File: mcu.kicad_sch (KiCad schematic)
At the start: 58 parts, among them P20 HEADER-2x11, P22 HEADER-2x13, P26 LPC_JTAG, P28 HEADER-2x11, SW1 SWITCH, SW2 SWITCH, U20 W25Q16, U23 LPC4330FET180, X2 MCU_XTAL, X3 RTC_XTAL

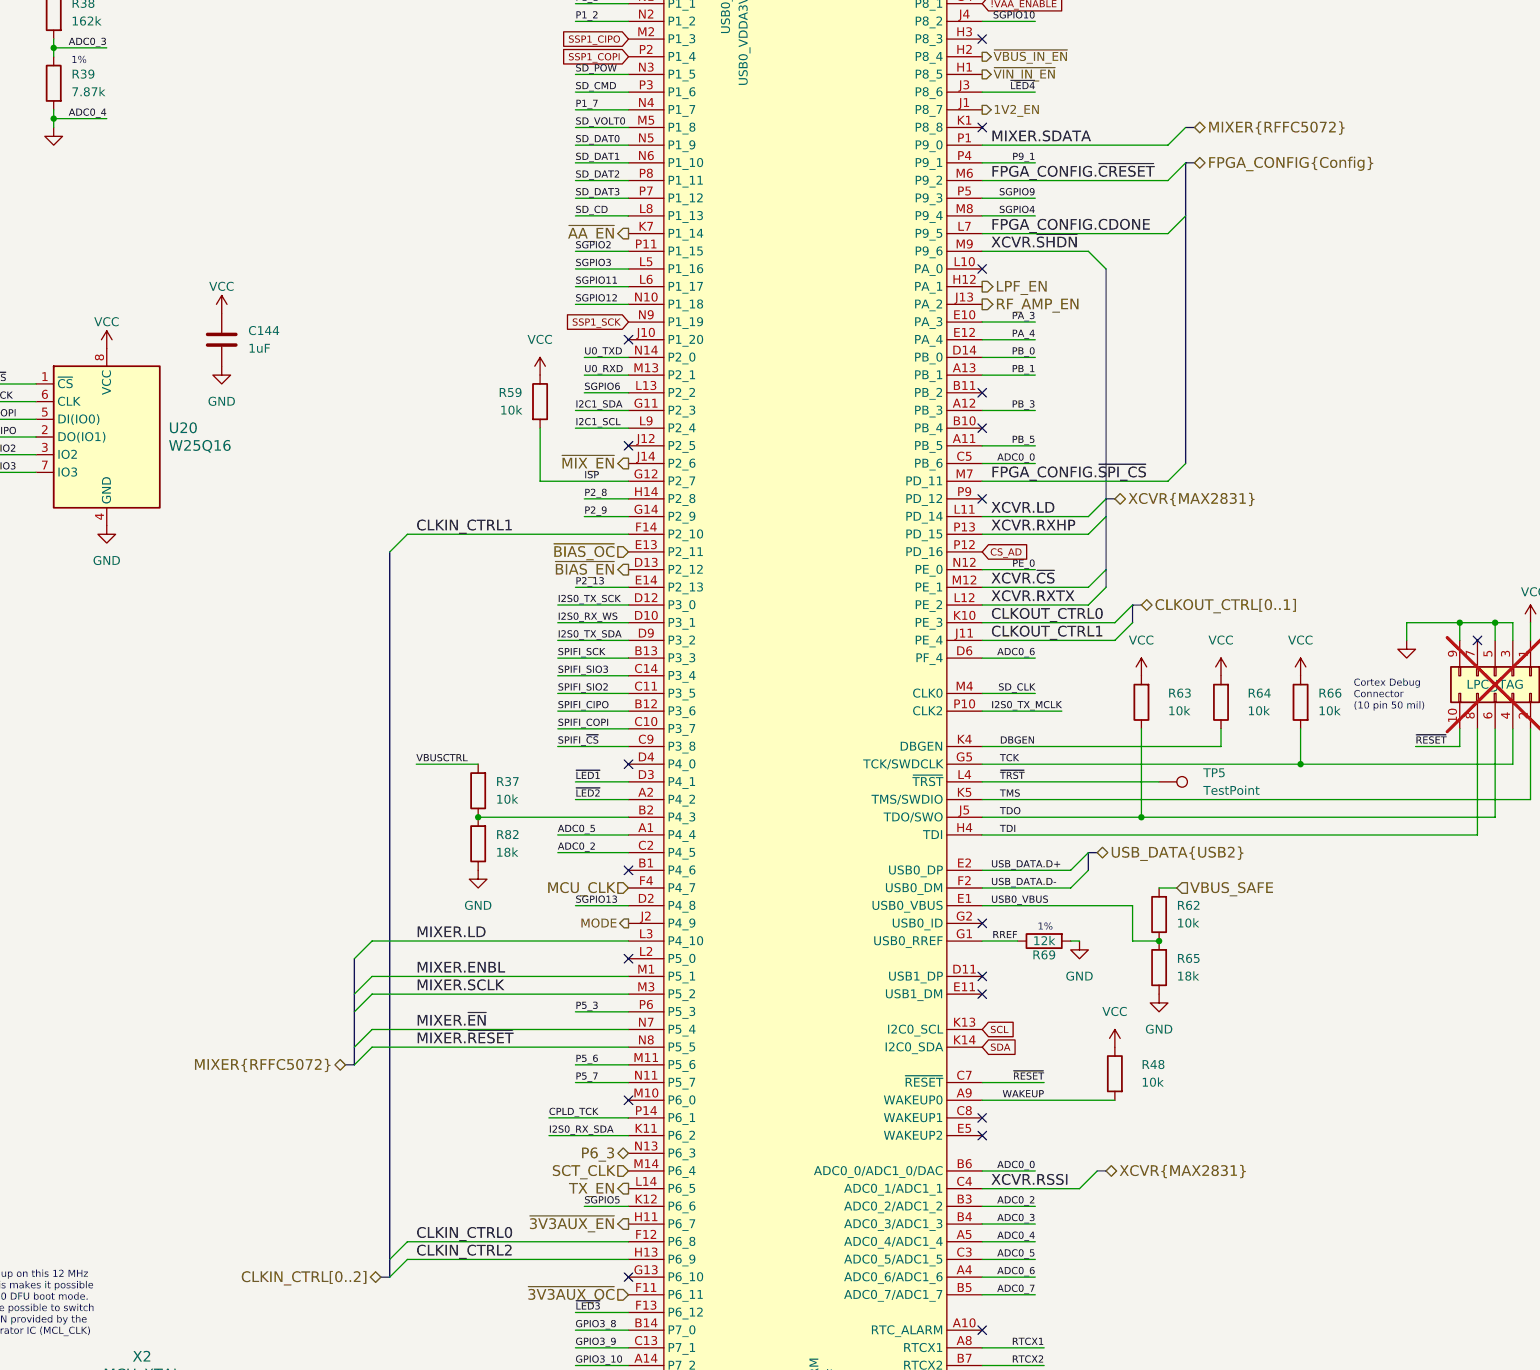
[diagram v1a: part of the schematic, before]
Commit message: Adjust position of FPGA U16
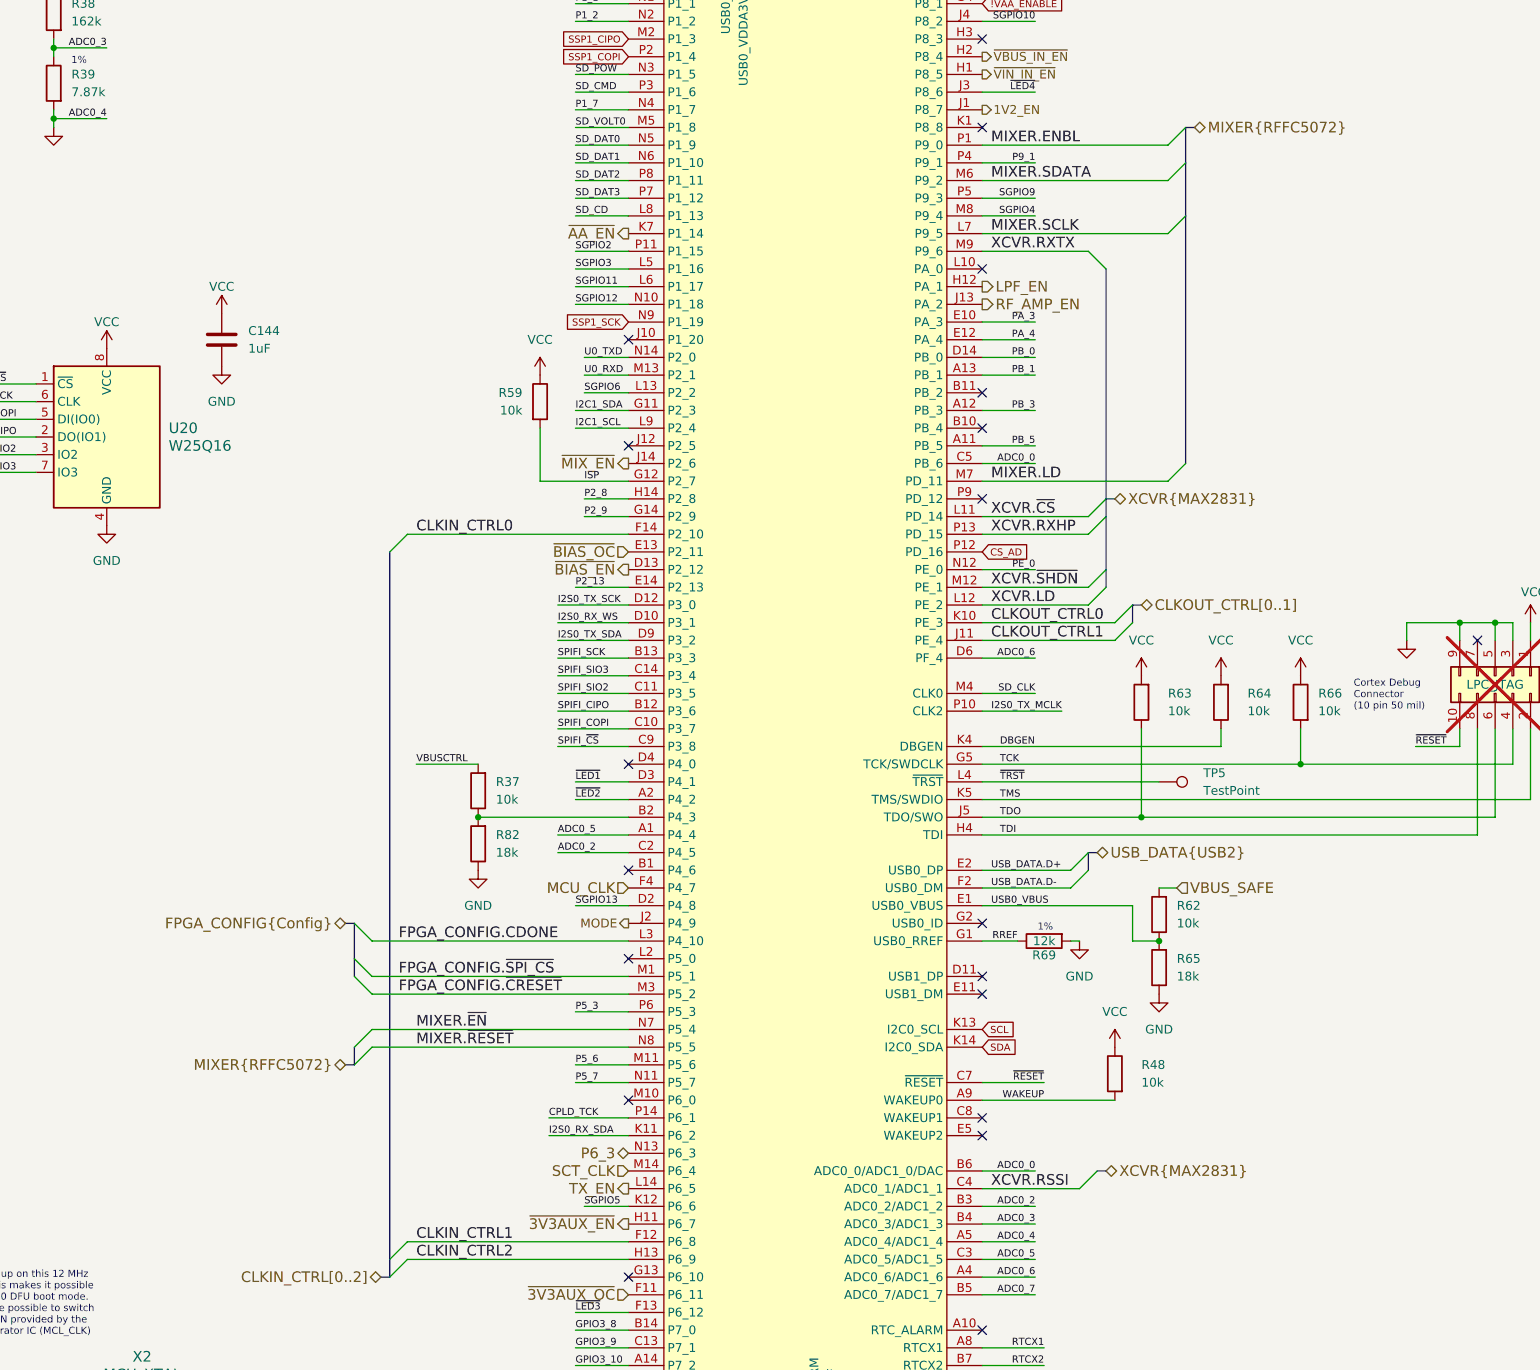
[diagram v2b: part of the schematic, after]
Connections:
- net CLKIN_CTRL0: now also U23.F14 (P2_10); no longer U23.F12 (P6_8)
- net CLKIN_CTRL1: now also U23.F12 (P6_8); no longer U23.F14 (P2_10)
- net FPGA_CONFIG.CDONE: now also U23.L3 (P4_10); no longer U23.L7 (P9_5)
- net FPGA_CONFIG.~{CRESET}: now also U23.M3 (P5_2); no longer U23.M6 (P9_2)
- net FPGA_CONFIG.~{SPI_CS}: now also U23.M1 (P5_1); no longer U23.M7 (PD_11)
- net MIXER.ENBL: now also U23.P1 (P9_0); no longer U23.M1 (P5_1)
- net MIXER.LD: now also U23.M7 (PD_11); no longer U23.L3 (P4_10)
- net MIXER.SCLK: now also U23.L7 (P9_5); no longer U23.M3 (P5_2)
- net MIXER.SDATA: now also U23.M6 (P9_2); no longer U23.P1 (P9_0)
- net XCVR.LD: now also U23.L12 (PE_2); no longer U23.L11 (PD_14)
- net XCVR.RXTX: now also U23.M9 (P9_6); no longer U23.L12 (PE_2)
- net XCVR.~{CS}: now also U23.L11 (PD_14); no longer U23.M12 (PE_1)
- net XCVR.~{SHDN}: now also U23.M12 (PE_1); no longer U23.M9 (P9_6)
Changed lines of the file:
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@@
 	)
 	(bus_entry
-		(at 154.94 185.42)
-		(size 2.54 -2.54)
-		(stroke
-			(width 0)
-			(type default)
-		)
-	)
-	(bus_entry
 		(at 368.3 44.45)
 		(size 2.54 2.54)
@@
 	)
 	(bus_entry
-		(at 154.94 187.96)
-		(size 2.54 -2.54)
+		(at 157.48 185.42)
+		(size -2.54 -2.54)
 		(stroke
 			(width 0)
@@
 	)
 	(bus_entry
-		(at 154.94 180.34)
-		(size 2.54 -2.54)
+		(at 157.48 177.8)
+		(size -2.54 -2.54)
 		(stroke
 			(width 0)
@@
 	)
 	(bus_entry
+		(at 157.48 182.88)
+		(size -2.54 -2.54)
+		(stroke
+			(width 0)
+			(type default)
+		)
+	)
+	(bus_entry
 		(at 160.02 223.52)
 		(size 2.54 -2.54)
@@
 		)
 	)
+	(bus
+		(pts
+			(xy 154.94 175.26) (xy 154.94 180.34)
+		)
+		(stroke
+			(width 0)
+			(type default)
+		)
+	)
 	(wire
 		(pts
@@
 	(bus
 		(pts
-			(xy 264.16 114.3) (xy 262.89 114.3)
+			(xy 153.67 175.26) (xy 154.94 175.26)
 		)
 		(stroke
@@
 	(bus
 		(pts
-			(xy 274.32 66.04) (xy 274.32 73.66)
+			(xy 264.16 114.3) (xy 262.89 114.3)
 		)
 		(stroke
@@
 		)
 	)
-	(bus
-		(pts
-			(xy 274.32 73.66) (xy 274.32 109.22)
-		)
-		(stroke
-			(width 0)
-			(type default)
-		)
-	)
 	(wire
 		(pts
@@
 	(bus
 		(pts
+			(xy 154.94 180.34) (xy 154.94 182.88)
+		)
+		(stroke
+			(width 0)
+			(type default)
+		)
+	)
+	(bus
+		(pts
 			(xy 260.35 167.64) (xy 260.35 165.1)
 		)
@@
 		)
 	)
-	(bus
-		(pts
-			(xy 154.94 187.96) (xy 154.94 193.04)
-		)
-		(stroke
-			(width 0)
-			(type default)
-		)
-	)
 	(wire
 		(pts
@@
 		)
 	)
-	(bus
-		(pts
-			(xy 274.32 66.04) (xy 275.59 66.04)
-		)
-		(stroke
-			(width 0)
-			(type default)
-		)
-	)
 	(wire
 		(pts
@@
 		)
 	)
-	(bus
+	(wire
 		(pts
-			(xy 154.94 185.42) (xy 154.94 187.96)
+			(xy 95.25 39.37) (xy 101.6 39.37)
 		)
 		(stroke
@@
 	(wire
 		(pts
-			(xy 95.25 39.37) (xy 101.6 39.37)
+			(xy 350.52 139.7) (xy 361.95 139.7)
 		)
 		(stroke
@@
 		)
 	)
-	(wire
+	(bus
 		(pts
-			(xy 350.52 139.7) (xy 361.95 139.7)
+			(xy 274.32 73.66) (xy 274.32 109.22)
 		)
 		(stroke
@@
 		)
 	)
-	(bus
-		(pts
-			(xy 154.94 180.34) (xy 154.94 185.42)
-		)
-		(stroke
-			(width 0)
-			(type default)
-		)
-	)
 	(wire
 		(pts
@@
 		)
 	)
+	(bus
+		(pts
+			(xy 274.32 60.96) (xy 274.32 66.04)
+		)
+		(stroke
+			(width 0)
+			(type default)
+		)
+	)
 	(wire
 		(pts
@@
 		)
 	)
+	(bus
+		(pts
+			(xy 274.32 66.04) (xy 274.32 73.66)
+		)
+		(stroke
+			(width 0)
+			(type default)
+		)
+	)
 	(wire
 		(pts
@@
 	)
 	(label "FPGA_CONFIG.~{SPI_CS}"
-		(at 246.38 111.76 0)
+		(at 161.29 182.88 0)
 		(effects
 			(font
@@
 	)
 	(label "XCVR.~{SHDN}"
-		(at 246.38 78.74 0)
+		(at 246.38 127 0)
 		(effects
 			(font
@@
 	)
 	(label "CLKIN_CTRL0"
-		(at 163.83 220.98 0)
+		(at 163.83 119.38 0)
 		(effects
 			(font
@@
 	)
 	(label "FPGA_CONFIG.~{CRESET}"
-		(at 246.38 68.58 0)
+		(at 161.29 185.42 0)
 		(effects
 			(font
@@
 	)
 	(label "CLKIN_CTRL1"
-		(at 163.83 119.38 0)
+		(at 163.83 220.98 0)
 		(effects
 			(font
@@
 	)
 	(label "XCVR.RXTX"
-		(at 246.38 129.54 0)
+		(at 246.38 78.74 0)
 		(effects
 			(font
@@
 	)
 	(label "XCVR.LD"
-		(at 246.38 116.84 0)
+		(at 246.38 129.54 0)
 		(effects
 			(font
@@
 	)
 	(label "FPGA_CONFIG.CDONE"
-		(at 246.38 76.2 0)
+		(at 161.29 177.8 0)
 		(effects
 			(font
@@
 	)
 	(label "XCVR.~{CS}"
-		(at 246.38 127 0)
+		(at 246.38 116.84 0)
 		(effects
 			(font
@@
 	)
 	(label "MIXER.SDATA"
-		(at 246.38 63.5 0)
+		(at 246.38 68.58 0)
 		(effects
 			(font
@@
 	)
 	(label "MIXER.ENBL"
-		(at 163.83 182.88 0)
+		(at 246.38 63.5 0)
 		(effects
 			(font
@@
 	)
 	(label "MIXER.SCLK"
-		(at 163.83 185.42 0)
+		(at 246.38 76.2 0)
 		(effects
 			(font
@@
 	)
 	(label "MIXER.LD"
-		(at 163.83 177.8 0)
+		(at 246.38 111.76 0)
 		(effects
 			(font
@@
 		)
 	)
-	(hierarchical_label "FPGA_CONFIG{Config}"
-		(shape bidirectional)
-		(at 275.59 66.04 0)
-		(effects
-			(font
-				(size 1.524 1.524)
-			)
-			(justify left)
-		)
-	)
 	(hierarchical_label "CLKOUT_CTRL[0..1]"
 		(shape bidirectional)
@@
 		(effects
 			(font
+				(size 1.524 1.524)
+			)
+			(justify right)
+		)
+	)
+	(hierarchical_label "FPGA_CONFIG{Config}"
+		(shape bidirectional)
+		(at 153.67 175.26 180)
+		(effects
+			(font

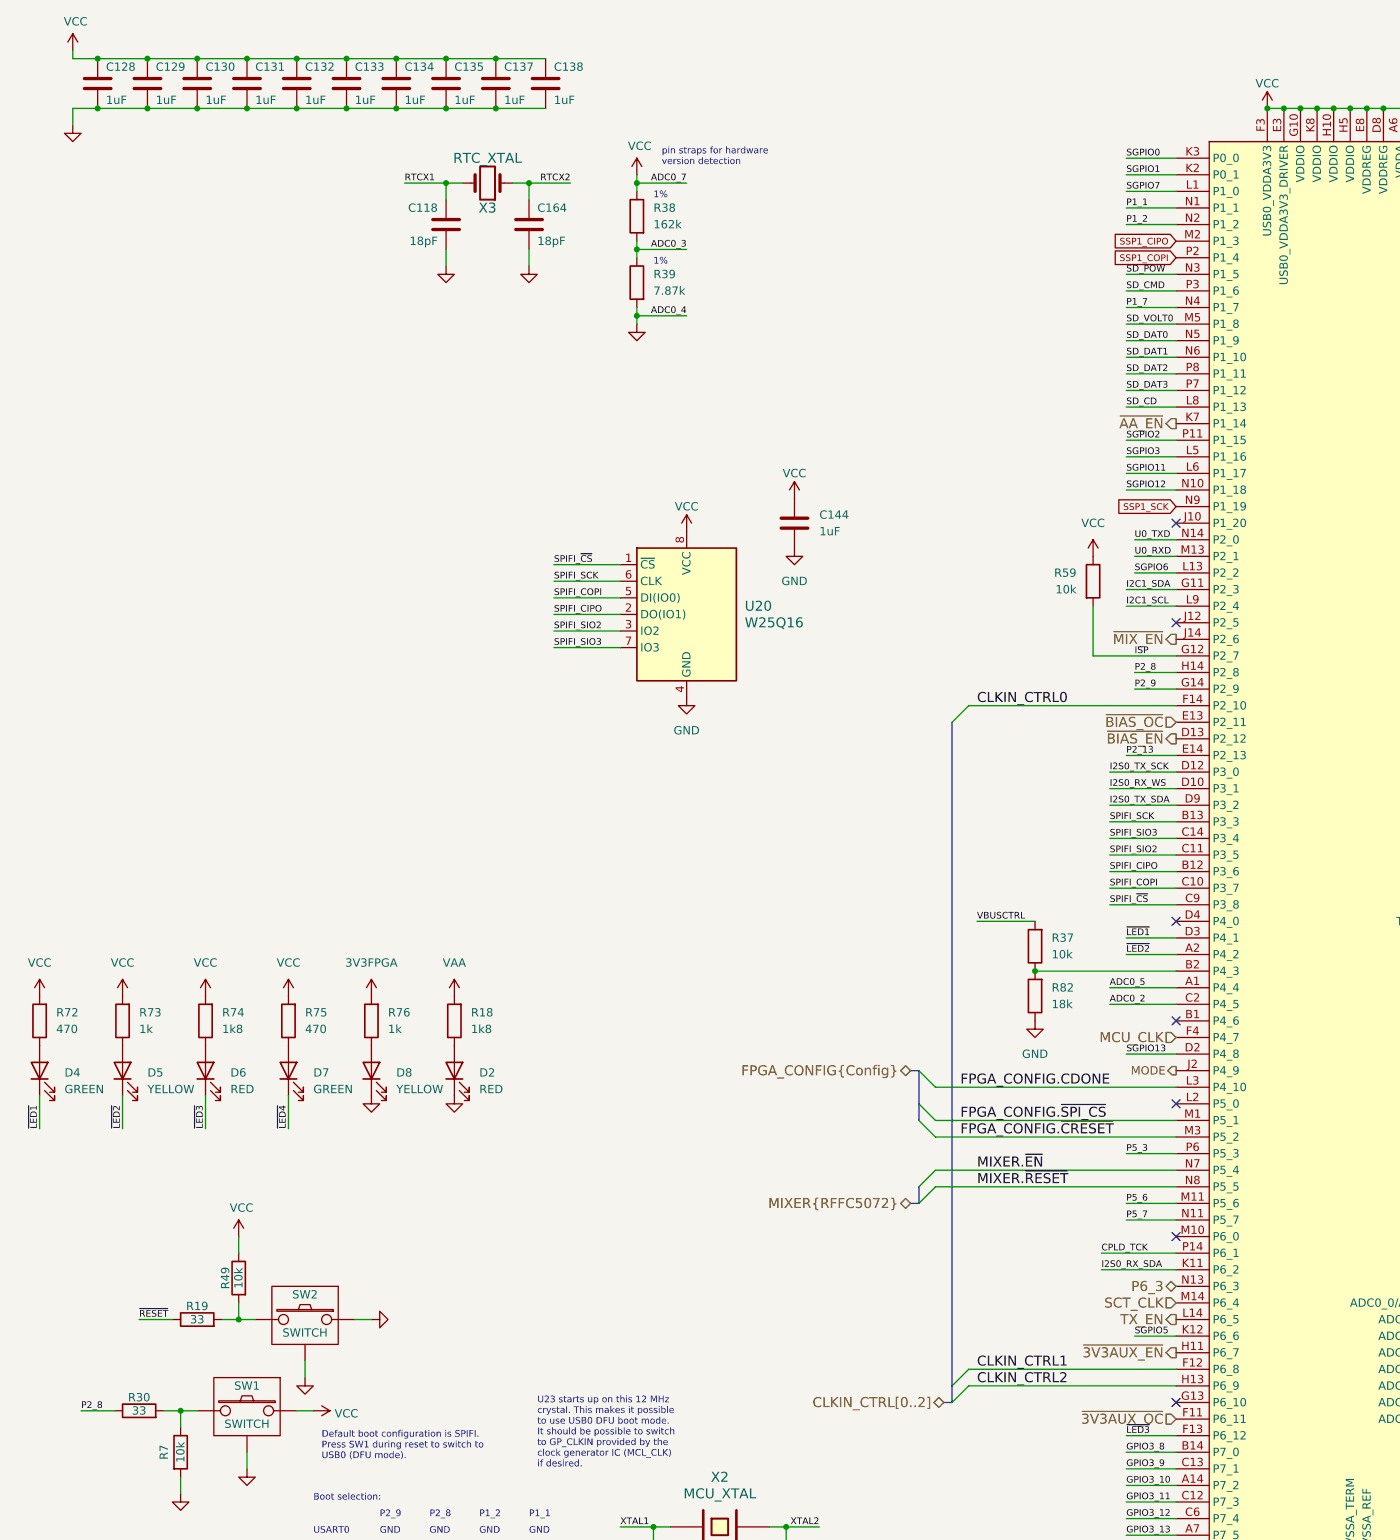
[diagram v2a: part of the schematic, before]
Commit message: Improve power supply filtering and decoupling
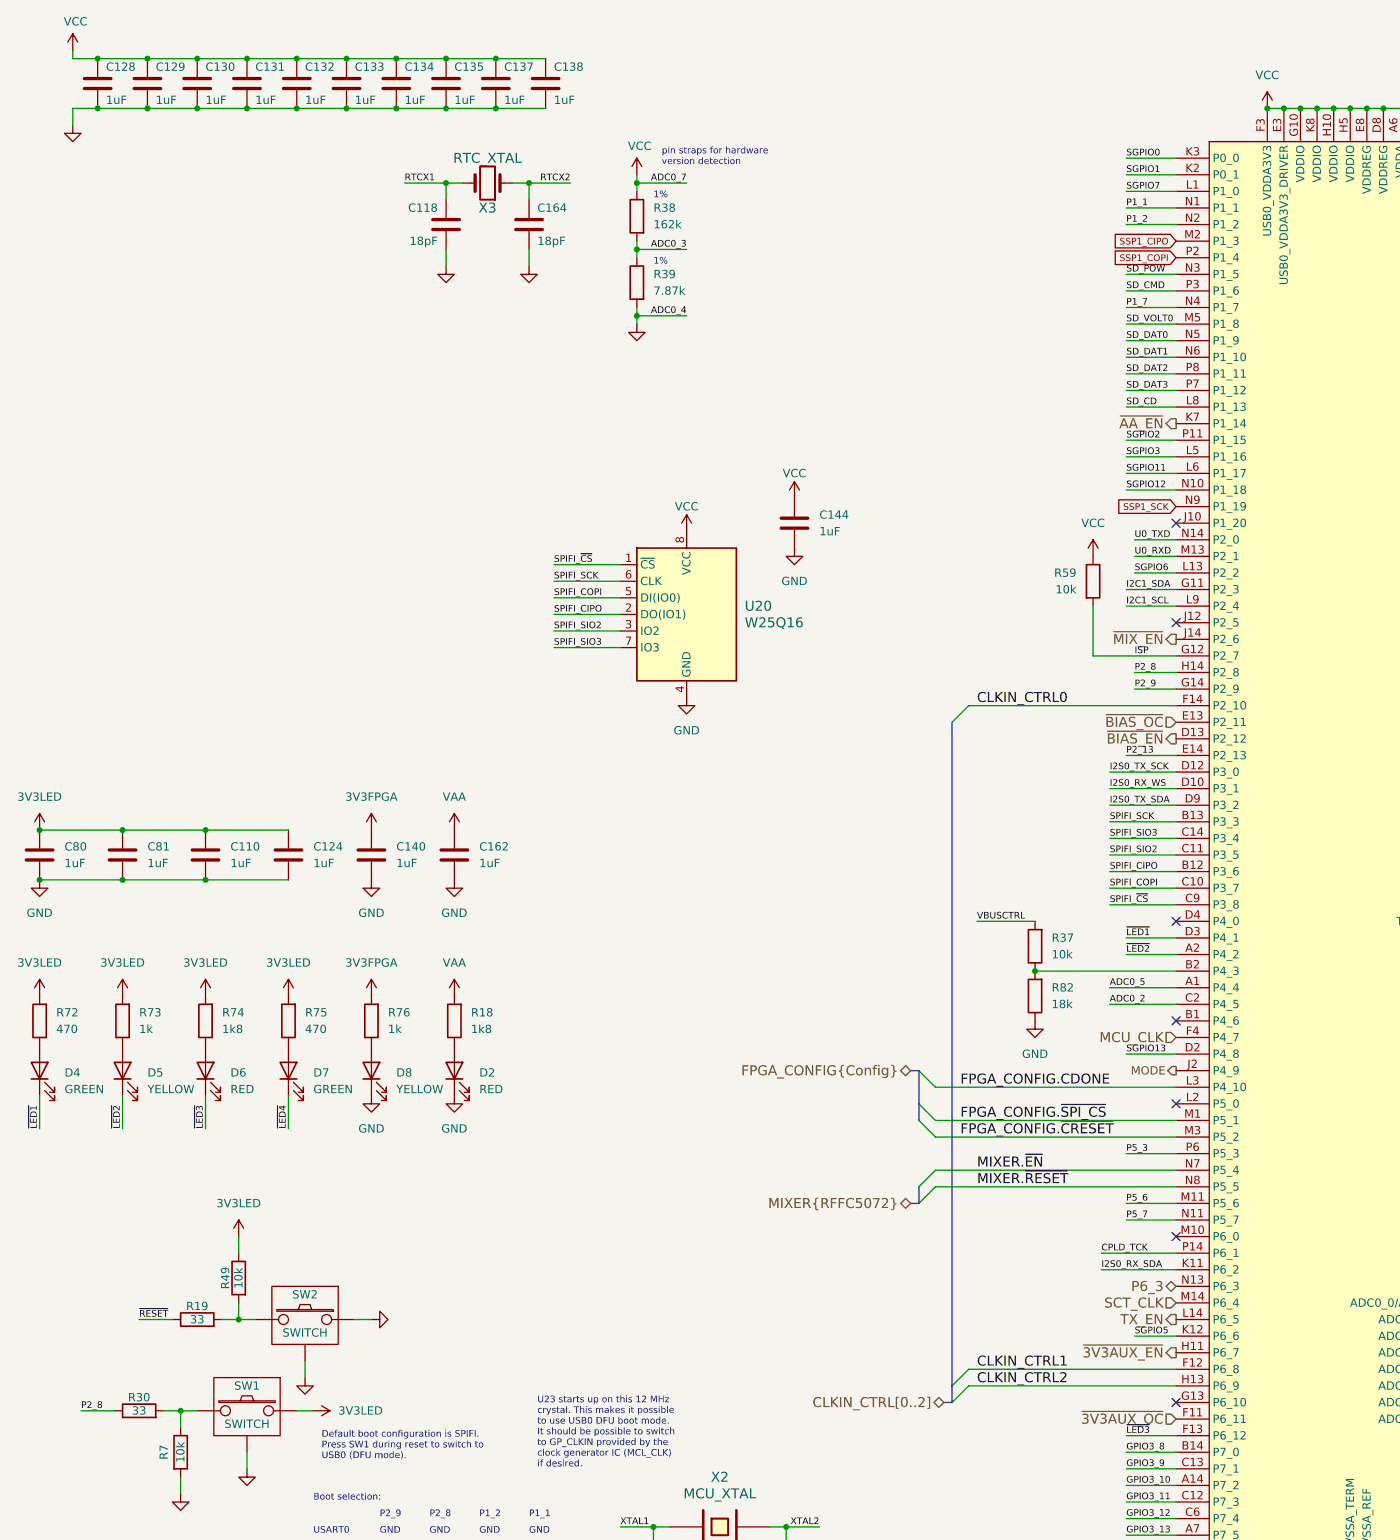
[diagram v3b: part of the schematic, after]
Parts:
- added C110, C124, C140, C162, C80, C81: 1uF, Capacitor_SMD:C_0402_1005Metric, symbol Device:C
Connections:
- net 3V3FPGA: now also C140.1
- net GND: now also C110.2, C124.2, C140.2, C162.2, C80.2, C81.2
- net VAA: now also C162.1
- net VCC: no longer R49.1, R72.2, R73.2, R74.2, R75.2, SW1.1
- new net 3V3LED: C110.1, C124.1, C80.1, C81.1, R49.1, R72.2, R73.2, R74.2, R75.2, SW1.1
